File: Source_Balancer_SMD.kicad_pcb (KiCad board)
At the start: 2 copper layers, 75 x 53 mm, 50 parts, among them J1 Screw_Terminal_01x01, J2 Screw_Terminal_01x01, J3 Screw_Terminal_01x01, J4 Screw_Terminal_01x01, J5 Conn_01x02_Male, Q1 2N4401, Q10 SQM10250E_GE3, Q2 2N4401, Q3 2N4401, Q4 2N4403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

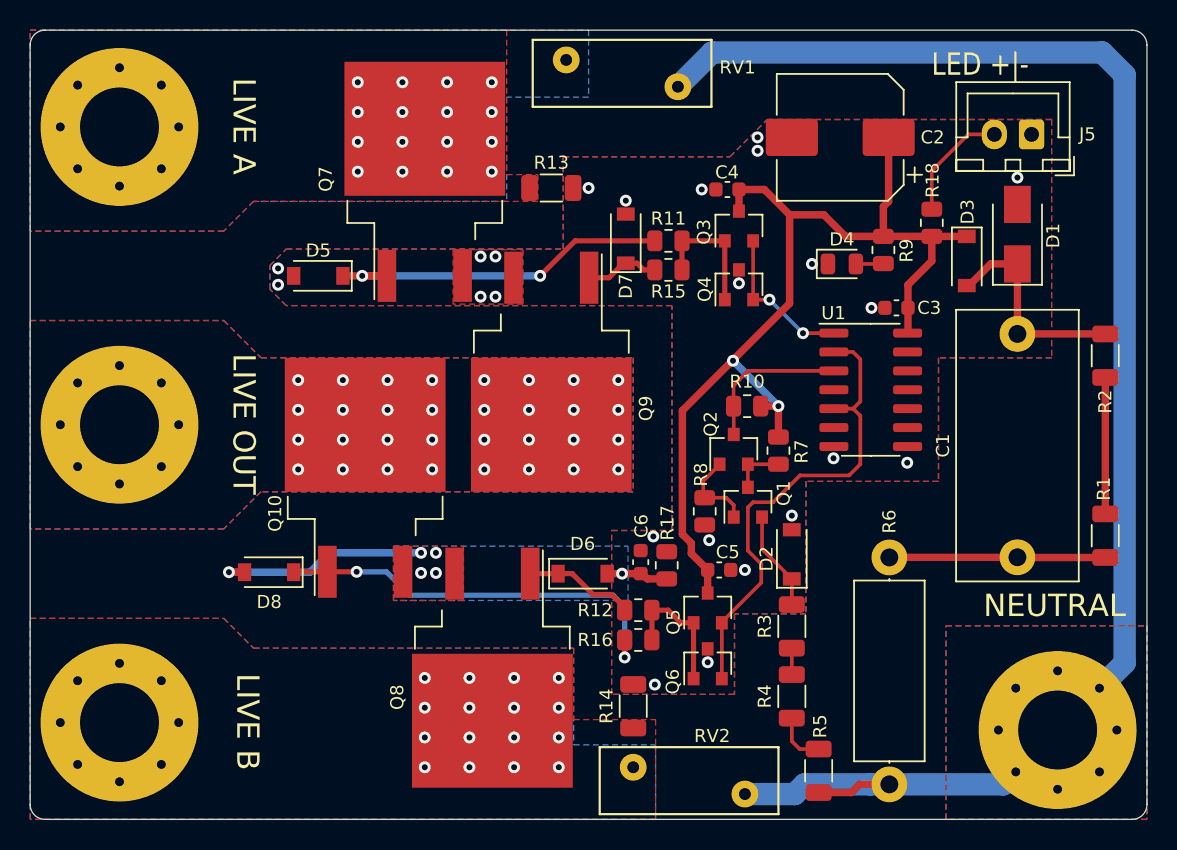
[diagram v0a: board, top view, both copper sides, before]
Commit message: BJTs are messed up
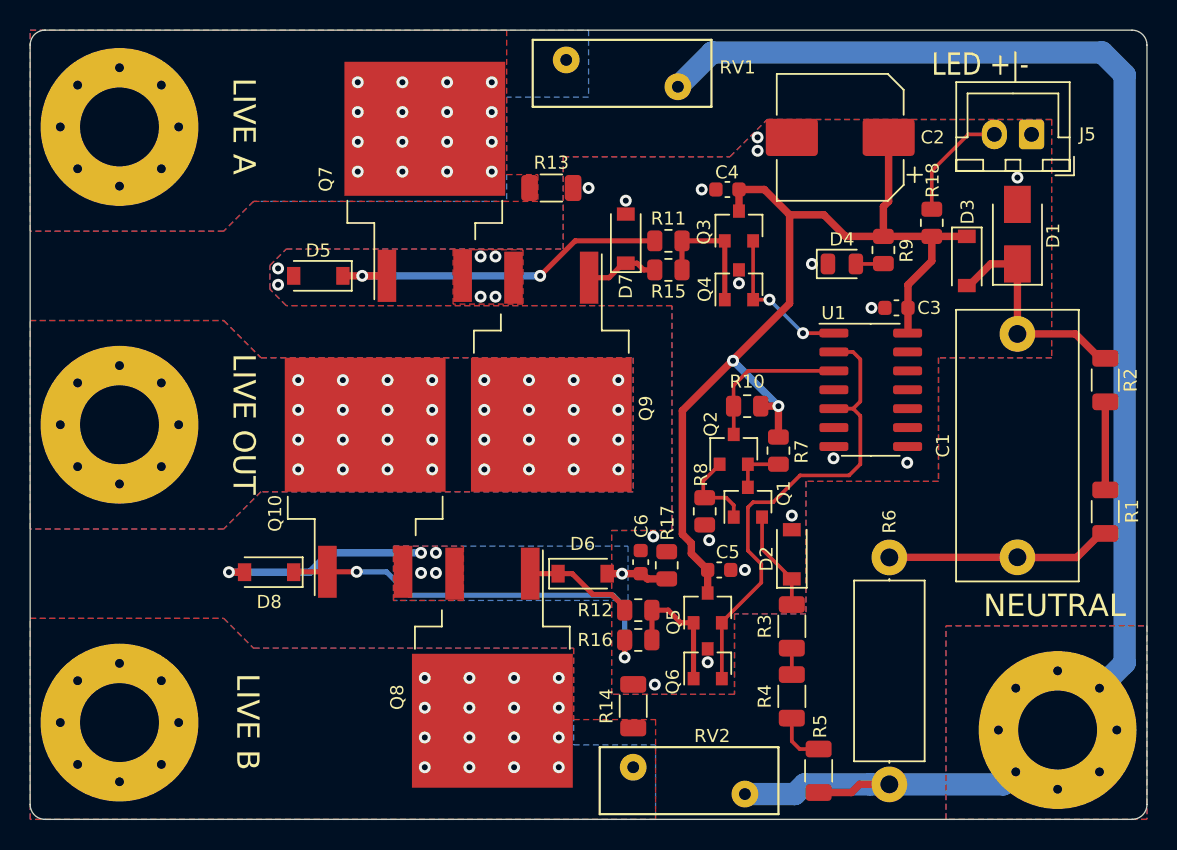
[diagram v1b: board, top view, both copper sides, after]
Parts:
- moved R2 1.64 mm to (131.2, 62.0)
- moved R1 1.61 mm to (131.2, 70.8)
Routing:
- net Net-(R1-Pad2): track 9.16 -> 5.91 mm
- net Net-(C1-Pad2): track 14.6 -> 15.3 mm
- net Net-(C1-Pad1): track 14.5 -> 15.2 mm
